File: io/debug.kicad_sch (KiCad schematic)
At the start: 14 parts, among them J11 Conn_02x03_Odd_Even, J12 Conn_02x06_Odd_Even, J4 Conn_02x03_Odd_Even, J5 Conn_02x04_Odd_Even, J6 Conn_02x12_Top_Bottom, J7 Conn_02x03_Odd_Even

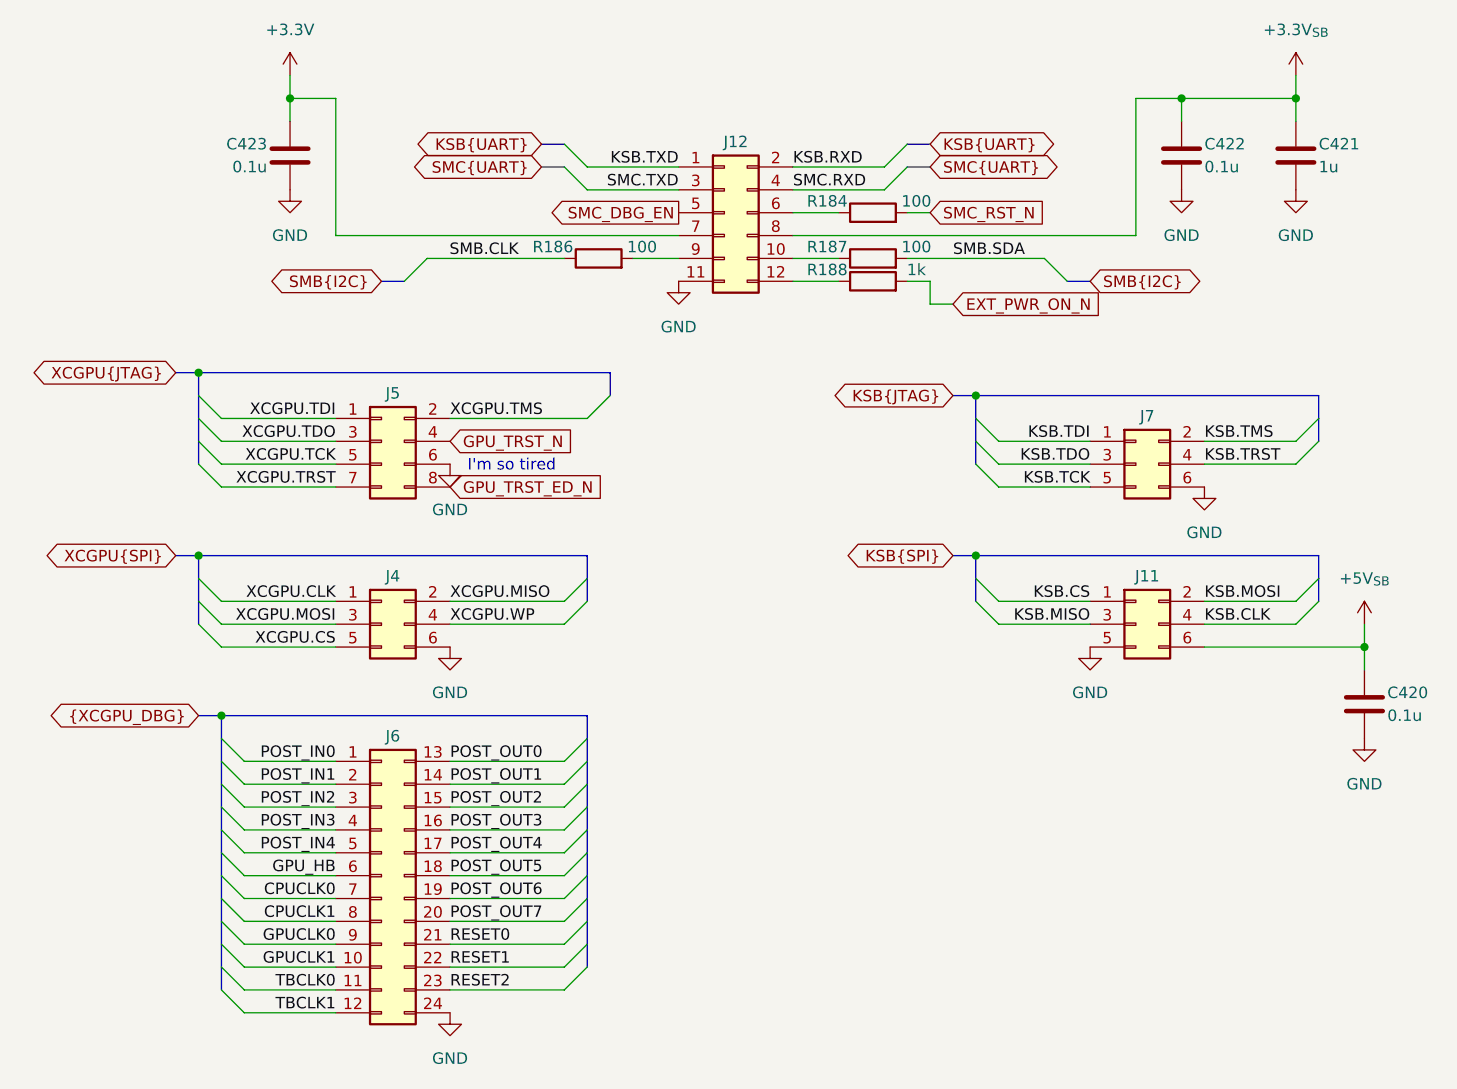
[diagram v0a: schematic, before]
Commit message: Multipurpose and standby power rails, Reannotated schematic
Added V_1P2, V_1P8, V_5P0DUAL, V_EFUSE, V_GPUPCIE, V_3P3STBY and V_1P2STBY
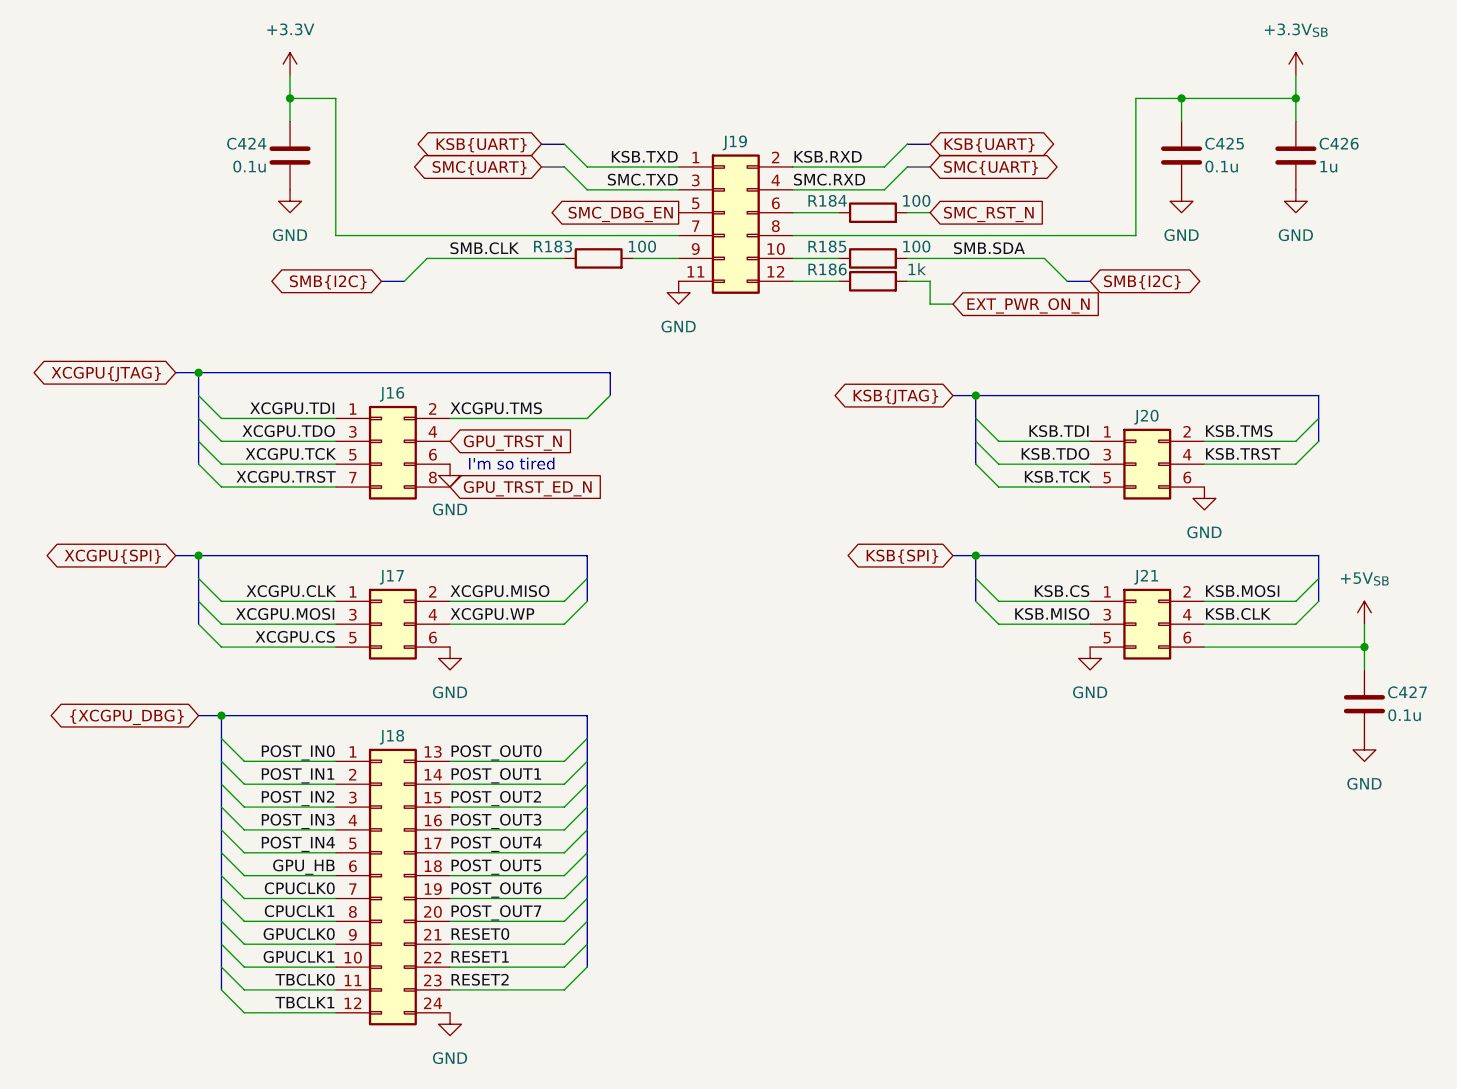
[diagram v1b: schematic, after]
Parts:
- renumbered C423 to C424, C422 to C425, C421 to C426, C420 to C427, J5 to J16, J4 to J17, J6 to J18, J12 to J19, J7 to J20, J11 to J21, R186 to R183, R187 to R185, R188 to R186
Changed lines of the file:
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@@
 		(dnp no)
 		(fields_autoplaced yes)
-		(property "Reference" "#PWR0388"
+		(property "Reference" "#PWR0402"
 			(at 93.98 50.8 0)
 			(effects
@@
 			(project "Mantaray"
 				(path "/16640ecb-e4a4-4594-871b-70047bfba6e0/f73644f9-7031-46ce-a27d-051daa072fe8"
-					(reference "#PWR0388")
+					(reference "#PWR0402")
 					(unit 1)
 				)
@@
 		(dnp no)
 		(fields_autoplaced yes)
-		(property "Reference" "#PWR0234"
+		(property "Reference" "#PWR0400"
 			(at 68.58 91.44 0)
 			(effects
@@
 			(project "Mantaray"
 				(path "/16640ecb-e4a4-4594-871b-70047bfba6e0/f73644f9-7031-46ce-a27d-051daa072fe8"
-					(reference "#PWR0234")
+					(reference "#PWR0400")
 					(unit 1)
 				)
@@
 		(on_board yes)
 		(dnp no)
-		(property "Reference" "J4"
+		(property "Reference" "J17"
 			(at 62.23 77.216 0)
 			(effects
@@
 			(project "Mantaray"
 				(path "/16640ecb-e4a4-4594-871b-70047bfba6e0/f73644f9-7031-46ce-a27d-051daa072fe8"
-					(reference "J4")
+					(reference "J17")
 					(unit 1)
 				)
@@
 		(dnp no)
 		(fields_autoplaced yes)
-		(property "Reference" "#PWR0384"
+		(property "Reference" "#PWR0407"
 			(at 162.56 40.64 0)
 			(effects
@@
 			(project "Mantaray"
 				(path "/16640ecb-e4a4-4594-871b-70047bfba6e0/f73644f9-7031-46ce-a27d-051daa072fe8"
-					(reference "#PWR0384")
+					(reference "#PWR0407")
 					(unit 1)
 				)
@@
 		(on_board yes)
 		(dnp no)
-		(property "Reference" "C420"
+		(property "Reference" "C427"
 			(at 172.72 90.17 0)
 			(effects
@@
 			(project "Mantaray"
 				(path "/16640ecb-e4a4-4594-871b-70047bfba6e0/f73644f9-7031-46ce-a27d-051daa072fe8"
-					(reference "C420")
+					(reference "C427")
 					(unit 1)
 				)
@@
 		(on_board yes)
 		(dnp no)
-		(property "Reference" "C423"
+		(property "Reference" "C424"
 			(at 48.26 29.21 0)
 			(effects
@@
 			(project "Mantaray"
 				(path "/16640ecb-e4a4-4594-871b-70047bfba6e0/f73644f9-7031-46ce-a27d-051daa072fe8"
-					(reference "C423")
+					(reference "C424")
 					(unit 1)
 				)
@@
 		(dnp no)
 		(fields_autoplaced yes)
-		(property "Reference" "#PWR0386"
+		(property "Reference" "#PWR0398"
 			(at 50.8 40.64 0)
 			(effects
@@
 			(project "Mantaray"
 				(path "/16640ecb-e4a4-4594-871b-70047bfba6e0/f73644f9-7031-46ce-a27d-051daa072fe8"
-					(reference "#PWR0386")
+					(reference "#PWR0398")
 					(unit 1)
 				)
@@
 		(dnp no)
 		(fields_autoplaced yes)
-		(property "Reference" "#PWR0387"
+		(property "Reference" "#PWR0397"
 			(at 50.8 25.4 0)
 			(effects
@@
 			(project "Mantaray"
 				(path "/16640ecb-e4a4-4594-871b-70047bfba6e0/f73644f9-7031-46ce-a27d-051daa072fe8"
-					(reference "#PWR0387")
+					(reference "#PWR0397")
 					(unit 1)
 				)
@@
 		(on_board yes)
 		(dnp no)
-		(property "Reference" "R186"
+		(property "Reference" "R183"
 			(at 80.01 40.64 90)
 			(effects
@@
 			(project "Mantaray"
 				(path "/16640ecb-e4a4-4594-871b-70047bfba6e0/f73644f9-7031-46ce-a27d-051daa072fe8"
-					(reference "R186")
+					(reference "R183")
 					(unit 1)
 				)
@@
 		(on_board yes)
 		(dnp no)
-		(property "Reference" "J11"
+		(property "Reference" "J21"
 			(at 146.05 77.216 0)
 			(effects
@@
 			(project "Mantaray"
 				(path "/16640ecb-e4a4-4594-871b-70047bfba6e0/f73644f9-7031-46ce-a27d-051daa072fe8"
-					(reference "J11")
+					(reference "J21")
 					(unit 1)
 				)
@@
 		(on_board yes)
 		(dnp no)
-		(property "Reference" "J7"
+		(property "Reference" "J20"
 			(at 146.05 59.436 0)
 			(effects
@@
 			(project "Mantaray"
 				(path "/16640ecb-e4a4-4594-871b-70047bfba6e0/f73644f9-7031-46ce-a27d-051daa072fe8"
-					(reference "J7")
+					(reference "J20")
 					(unit 1)
 				)
@@
 		(on_board yes)
 		(dnp no)
-		(property "Reference" "J5"
+		(property "Reference" "J16"
 			(at 62.23 56.896 0)
 			(effects
@@
 			(project "Mantaray"
 				(path "/16640ecb-e4a4-4594-871b-70047bfba6e0/f73644f9-7031-46ce-a27d-051daa072fe8"
-					(reference "J5")
+					(reference "J16")
 					(unit 1)
 				)
@@
 		(dnp no)
 		(fields_autoplaced yes)
-		(property "Reference" "#PWR0378"
+		(property "Reference" "#PWR0409"
 			(at 170.18 101.6 0)
 			(effects
@@
 			(project "Mantaray"
 				(path "/16640ecb-e4a4-4594-871b-70047bfba6e0/f73644f9-7031-46ce-a27d-051daa072fe8"
-					(reference "#PWR0378")
+					(reference "#PWR0409")
 					(unit 1)
 				)
@@
 		(dnp no)
 		(fields_autoplaced yes)
-		(property "Reference" "#PWR035"
+		(property "Reference" "#PWR0401"
 			(at 68.58 132.08 0)
 			(effects
@@
 			(project "Mantaray"
 				(path "/16640ecb-e4a4-4594-871b-70047bfba6e0/f73644f9-7031-46ce-a27d-051daa072fe8"
-					(reference "#PWR035")
+					(reference "#PWR0401")
 					(unit 1)
 				)
@@
 		(dnp no)
 		(fields_autoplaced yes)
-		(property "Reference" "#PWR0377"
+		(property "Reference" "#PWR0408"
 			(at 170.18 86.36 0)
 			(effects
@@
 			(project "Mantaray"
 				(path "/16640ecb-e4a4-4594-871b-70047bfba6e0/f73644f9-7031-46ce-a27d-051daa072fe8"
-					(reference "#PWR0377")
+					(reference "#PWR0408")
 					(unit 1)
 				)
@@
 		(dnp no)
 		(fields_autoplaced yes)
-		(property "Reference" "#PWR0257"
+		(property "Reference" "#PWR0405"
 			(at 152.4 73.66 0)
 			(effects
@@
 			(project "Mantaray"
 				(path "/16640ecb-e4a4-4594-871b-70047bfba6e0/f73644f9-7031-46ce-a27d-051daa072fe8"
-					(reference "#PWR0257")
+					(reference "#PWR0405")
 					(unit 1)
 				)
@@
 		(dnp no)
 		(fields_autoplaced yes)
-		(property "Reference" "#PWR0385"
+		(property "Reference" "#PWR0404"
 			(at 149.86 40.64 0)
 			(effects
@@
 			(project "Mantaray"
 				(path "/16640ecb-e4a4-4594-871b-70047bfba6e0/f73644f9-7031-46ce-a27d-051daa072fe8"
-					(reference "#PWR0385")
+					(reference "#PWR0404")
 					(unit 1)
 				)
@@
 		(on_board yes)
 		(dnp no)
-		(property "Reference" "J12"
+		(property "Reference" "J19"
 			(at 100.33 28.956 0)
 			(effects
@@
 			(project ""
 				(path "/16640ecb-e4a4-4594-871b-70047bfba6e0/f73644f9-7031-46ce-a27d-051daa072fe8"
-					(reference "J12")
+					(reference "J19")
 					(unit 1)
 				)
@@
 		(on_board yes)
 		(dnp no)
-		(property "Reference" "C421"
+		(property "Reference" "C426"
 			(at 165.1 29.21 0)
 			(effects
@@
 			(project "Mantaray"
 				(path "/16640ecb-e4a4-4594-871b-70047bfba6e0/f73644f9-7031-46ce-a27d-051daa072fe8"
-					(reference "C421")
+					(reference "C426")
 					(unit 1)
 				)
@@
 		(on_board yes)
 		(dnp no)
-		(property "Reference" "J6"
+		(property "Reference" "J18"
 			(at 62.23 94.996 0)
 			(effects
@@
 			(project "Mantaray"
 				(path "/16640ecb-e4a4-4594-871b-70047bfba6e0/f73644f9-7031-46ce-a27d-051daa072fe8"
-					(reference "J6")
+					(reference "J18")
 					(unit 1)
 				)
@@
 		(on_board yes)
 		(dnp no)
-		(property "Reference" "R187"
+		(property "Reference" "R185"
 			(at 110.49 40.64 90)
 			(effects
@@
 			(project "Mantaray"
 				(path "/16640ecb-e4a4-4594-871b-70047bfba6e0/f73644f9-7031-46ce-a27d-051daa072fe8"
-					(reference "R187")
+					(reference "R185")
 					(unit 1)
 				)
@@
 		(dnp no)
 		(fields_autoplaced yes)
-		(property "Reference" "#PWR088"
+		(property "Reference" "#PWR0399"
 			(at 68.58 71.12 0)
 			(effects
@@
 			(project "Mantaray"
 				(path "/16640ecb-e4a4-4594-871b-70047bfba6e0/f73644f9-7031-46ce-a27d-051daa072fe8"
-					(reference "#PWR088")
+					(reference "#PWR0399")
 					(unit 1)
 				)
@@
 		(dnp no)
 		(fields_autoplaced yes)
-		(property "Reference" "#PWR0376"
+		(property "Reference" "#PWR0403"
 			(at 139.7 91.44 0)
 			(effects
@@
 			(project "Mantaray"
 				(path "/16640ecb-e4a4-4594-871b-70047bfba6e0/f73644f9-7031-46ce-a27d-051daa072fe8"
-					(reference "#PWR0376")
+					(reference "#PWR0403")
 					(unit 1)
 				)
@@
 		(on_board yes)
 		(dnp no)
-		(property "Reference" "R188"
+		(property "Reference" "R186"
 			(at 110.49 43.18 90)
 			(effects
@@
 			(project "Mantaray"
 				(path "/16640ecb-e4a4-4594-871b-70047bfba6e0/f73644f9-7031-46ce-a27d-051daa072fe8"
-					(reference "R188")
+					(reference "R186")
 					(unit 1)
 				)
@@
 		(on_board yes)
 		(dnp no)
-		(property "Reference" "C422"
+		(property "Reference" "C425"
 			(at 152.4 29.21 0)
 			(effects
@@
 			(project "Mantaray"
 				(path "/16640ecb-e4a4-4594-871b-70047bfba6e0/f73644f9-7031-46ce-a27d-051daa072fe8"
-					(reference "C422")
+					(reference "C425")
 					(unit 1)
 				)
@@
 		(dnp no)
 		(fields_autoplaced yes)
-		(property "Reference" "#PWR0383"
+		(property "Reference" "#PWR0406"
 			(at 162.56 25.4 0)
 			(effects
@@
 			(project "Mantaray"
 				(path "/16640ecb-e4a4-4594-871b-70047bfba6e0/f73644f9-7031-46ce-a27d-051daa072fe8"
-					(reference "#PWR0383")
-					(unit 1)
-				)
+					(reference "#PWR0406")
+					(unit 1)
+				)
